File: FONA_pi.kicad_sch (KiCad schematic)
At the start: 37 parts, among them J1 Conn_01x20_Socket, J10 Conn_01x04_Pin, J11 Conn_01x20_Socket, J12 Conn_01x20_Socket, J13 Conn_01x06_Socket, J14 Conn_01x06_Socket, J15 Conn_01x06_Socket, J16 Conn_01x06_Socket, J17 Conn_01x06_Socket, J18 Conn_01x04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

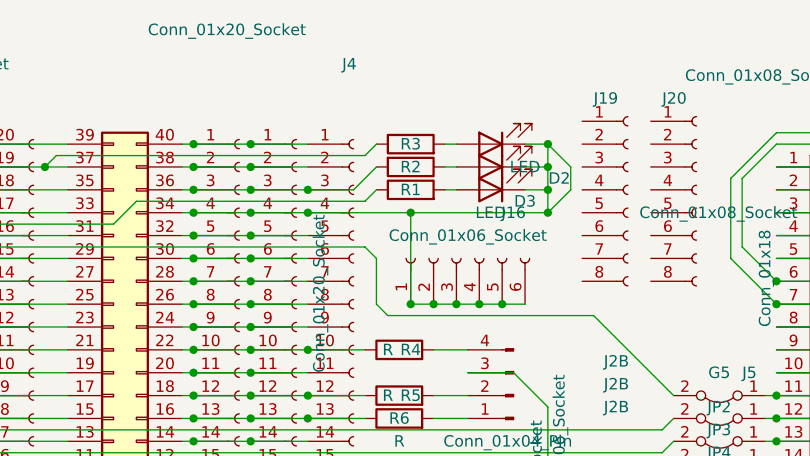
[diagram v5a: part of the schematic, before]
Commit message: Flipped a backwards resistor.  Added labels for LED colors, switch resistors
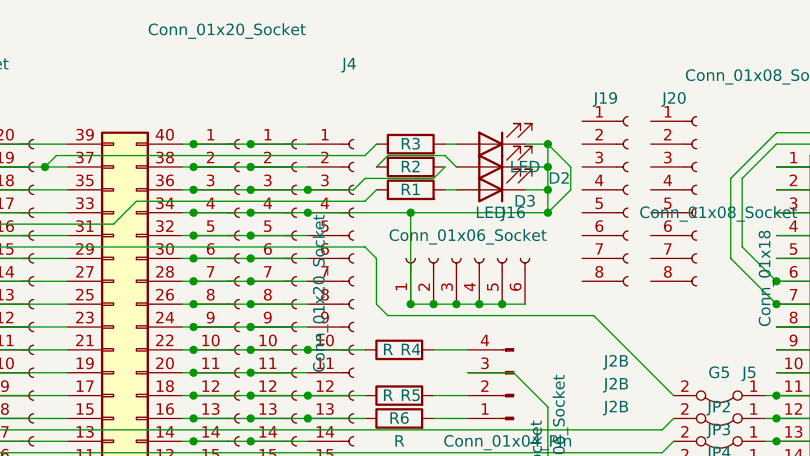
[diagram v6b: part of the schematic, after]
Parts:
- J6: footprint Connector_PinHeader_2.54mm:PinHeader_1x18_P2.54mm_Vertical -> Connector_PinSocket_2.54mm:PinSocket_1x18_P2.54mm_Vertical
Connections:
- net at J2.36 (Pin_36), J3.3 (Pin_3), J4.3 (Pin_3)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: now also R2.1; no longer R2.2
- net at D2.2 (A): now also R2.2; no longer R2.1
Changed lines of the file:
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@@
+    (stroke (width 0) (type default))
+  )
+  (wire (pts (xy 105.41 68.58) (xy 106.68 69.85))
     (stroke (width 0) (type default))
   )
@@
     (stroke (width 0) (type default))
   )
-  (wire (pts (xy 105.41 69.85) (xy 106.68 69.85))
-    (stroke (width 0) (type default))
-  )
   (wire (pts (xy 142.24 87.63) (xy 151.13 87.63))
     (stroke (width 0) (type default))
@@
     (stroke (width 0) (type default))
   )
+  (wire (pts (xy 99.06 68.58) (xy 105.41 68.58))
+    (stroke (width 0) (type default))
+  )
   (wire (pts (xy 97.79 106.68) (xy 102.87 106.68))
     (stroke (width 0) (type default))
@@
     (stroke (width 0) (type default))
   )
+  (wire (pts (xy 96.52 71.12) (xy 95.25 72.39))
+    (stroke (width 0) (type default))
+  )
   (wire (pts (xy 44.45 95.25) (xy 54.61 95.25))
     (stroke (width 0) (type default))
@@
     (stroke (width 0) (type default))
   )
+  (wire (pts (xy 105.41 69.85) (xy 104.14 71.12))
+    (stroke (width 0) (type default))
+  )
   (wire (pts (xy 151.13 77.47) (xy 157.48 77.47))
     (stroke (width 0) (type default))
@@
     (stroke (width 0) (type default))
   )
-  (wire (pts (xy 95.25 72.39) (xy 97.79 69.85))
-    (stroke (width 0) (type default))
-  )
   (wire (pts (xy 46.99 99.06) (xy 45.72 97.79))
     (stroke (width 0) (type default))
@@
     (stroke (width 0) (type default))
   )
+  (wire (pts (xy 104.14 71.12) (xy 96.52 71.12))
+    (stroke (width 0) (type default))
+  )
   (wire (pts (xy 77.47 80.01) (xy 83.82 80.01))
     (stroke (width 0) (type default))
@@
   )
   (wire (pts (xy 76.2 77.47) (xy 77.47 77.47))
+    (stroke (width 0) (type default))
+  )
+  (wire (pts (xy 97.79 69.85) (xy 99.06 68.58))
     (stroke (width 0) (type default))
   )
@@
       (effects (font (size 1.27 1.27)) (justify left))
     )
-    (property "Footprint" "Connector_PinHeader_2.54mm:PinHeader_1x18_P2.54mm_Vertical" (at 156.21 90.17 0)
-      (effects (font (size 1.27 1.27)) hide)
-    )
+    (property "Footprint" "Connector_PinSocket_2.54mm:PinSocket_1x18_P2.54mm_Vertical" (at 156.21 90.17 0)
+      (effects (font (size 1.27 1.27)) hide)
+    )

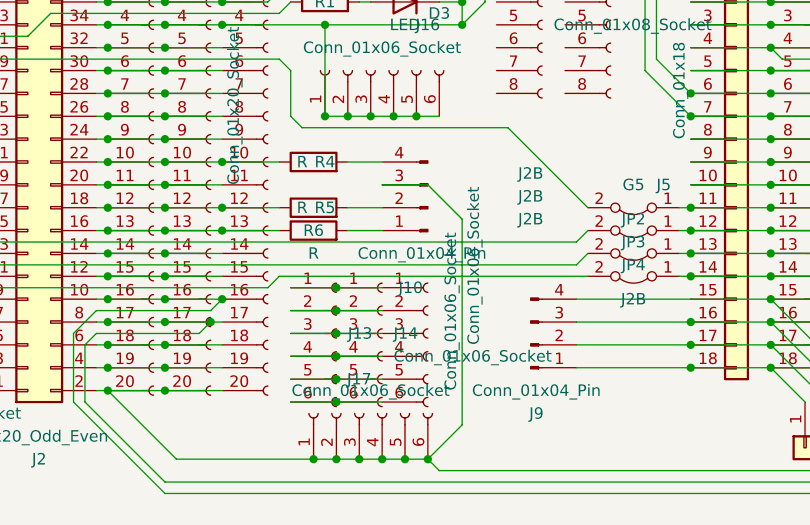
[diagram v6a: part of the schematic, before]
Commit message: Changed which wire of wire harness is used for power.  Now using the first wire from the top, which is a red wire on the harness, so that 5v power will be on the red wire
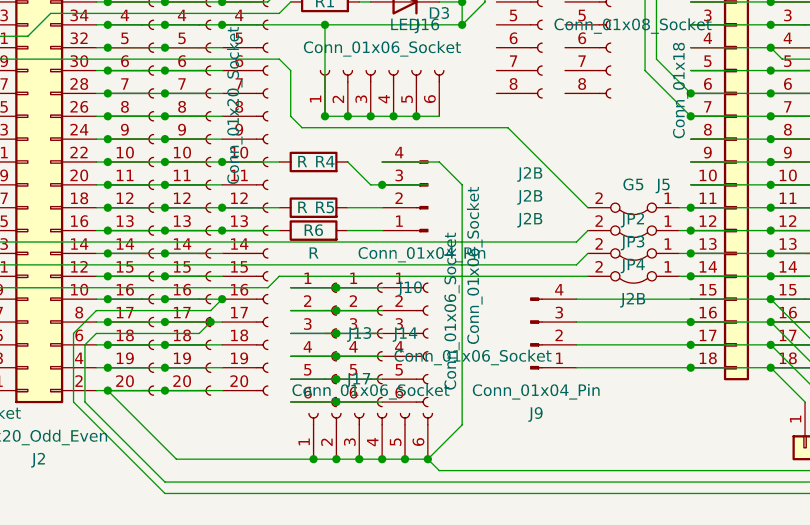
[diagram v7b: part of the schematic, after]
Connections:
- net at J17.1 (Pin_1), J17.2 (Pin_2), J17.3 (Pin_3)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: now also J10.4 (Pin_4); no longer J10.3 (Pin_3)
- net at R4.2: now also J10.3 (Pin_3); no longer J10.4 (Pin_4)
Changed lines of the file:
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@@
   (junction (at 151.13 85.09) (diameter 0) (color 0 0 0 0)
   )
+  (junction (at 107.95 92.71) (diameter 0) (color 0 0 0 0)
+  )
   (junction (at 54.61 105.41) (diameter 0) (color 0 0 0 0)
   )
@@
   (junction (at 83.82 72.39) (diameter 0) (color 0 0 0 0)
   )
-  (wire (pts (xy 104.14 90.17) (xy 107.95 90.17))
-    (stroke (width 0) (type default))
-  )
   (wire (pts (xy 45.72 97.79) (xy 54.61 97.79))
     (stroke (width 0) (type default))
@@
     (stroke (width 0) (type default))
   )
+  (wire (pts (xy 107.95 90.17) (xy 114.3 90.17))
+    (stroke (width 0) (type default))
+  )
   (wire (pts (xy 162.56 127) (xy 83.82 127))
     (stroke (width 0) (type default))
@@
     (stroke (width 0) (type default))
   )
-  (wire (pts (xy 116.84 96.52) (xy 116.84 119.38))
+  (wire (pts (xy 116.84 92.71) (xy 116.84 119.38))
     (stroke (width 0) (type default))
   )
@@
     (stroke (width 0) (type default))
   )
+  (wire (pts (xy 106.68 92.71) (xy 104.14 90.17))
+    (stroke (width 0) (type default))
+  )
   (wire (pts (xy 104.14 95.25) (xy 107.95 95.25))
     (stroke (width 0) (type default))
@@
     (stroke (width 0) (type default))
   )
-  (wire (pts (xy 113.03 92.71) (xy 116.84 96.52))
-    (stroke (width 0) (type default))
-  )
   (wire (pts (xy 137.16 71.12) (xy 142.24 66.04))
     (stroke (width 0) (type default))
@@
     (stroke (width 0) (type default))
   )
+  (wire (pts (xy 114.3 90.17) (xy 116.84 92.71))
+    (stroke (width 0) (type default))
+  )
   (wire (pts (xy 151.13 80.01) (xy 157.48 80.01))
     (stroke (width 0) (type default))
@@
     (stroke (width 0) (type default))
   )
+  (wire (pts (xy 107.95 92.71) (xy 106.68 92.71))
+    (stroke (width 0) (type default))
+  )

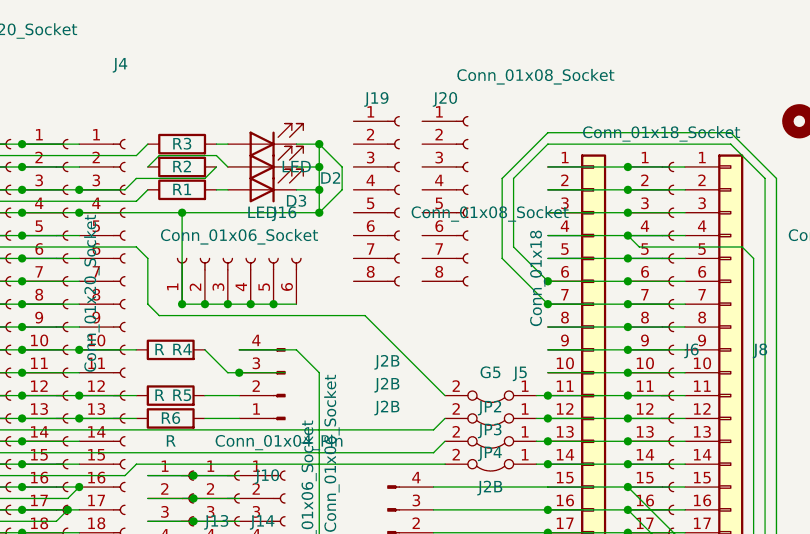
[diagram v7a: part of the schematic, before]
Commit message: Grounded FONA to Pi
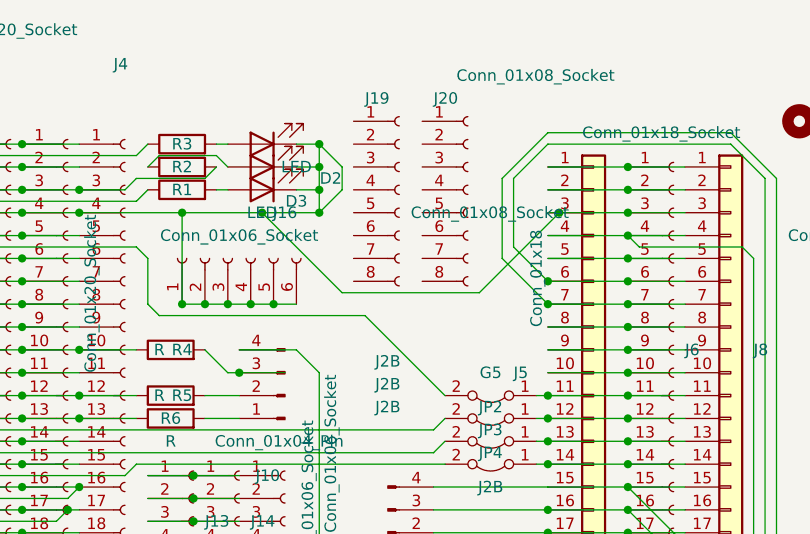
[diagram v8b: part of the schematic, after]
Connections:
- net at D1.1 (K), D2.1 (K), D3.1 (K)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: now also J5.3 (Pin_3), J6.3 (Pin_3), J8.3 (Pin_3)
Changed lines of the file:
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@@
   (junction (at 142.24 100.33) (diameter 0) (color 0 0 0 0)
   )
+  (junction (at 143.51 74.93) (diameter 0) (color 0 0 0 0)
+  )
   (junction (at 44.45 80.01) (diameter 0) (color 0 0 0 0)
   )
@@
   (junction (at 113.03 123.19) (diameter 0) (color 0 0 0 0)
   )
+  (junction (at 110.49 74.93) (diameter 0) (color 0 0 0 0)
+  )
   (junction (at 151.13 110.49) (diameter 0) (color 0 0 0 0)
   )
@@
     (stroke (width 0) (type default))
   )
-  (wire (pts (xy 142.24 74.93) (xy 151.13 74.93))
+  (wire (pts (xy 142.24 74.93) (xy 143.51 74.93))
     (stroke (width 0) (type default))
   )
@@
     (stroke (width 0) (type default))
   )
-  (wire (pts (xy 101.6 74.93) (xy 116.84 74.93))
+  (wire (pts (xy 101.6 74.93) (xy 110.49 74.93))
+    (stroke (width 0) (type default))
+  )
+  (wire (pts (xy 110.49 74.93) (xy 116.84 74.93))
     (stroke (width 0) (type default))
   )
@@
     (stroke (width 0) (type default))
   )
+  (wire (pts (xy 119.38 83.82) (xy 110.49 74.93))
+    (stroke (width 0) (type default))
+  )
   (wire (pts (xy 44.45 69.85) (xy 54.61 69.85))
     (stroke (width 0) (type default))
@@
     (stroke (width 0) (type default))
   )
+  (wire (pts (xy 143.51 74.93) (xy 134.62 83.82))
+    (stroke (width 0) (type default))
+  )
   (wire (pts (xy 54.61 85.09) (xy 63.5 85.09))
     (stroke (width 0) (type default))
@@
     (stroke (width 0) (type default))
   )
+  (wire (pts (xy 119.38 83.82) (xy 134.62 83.82))
+    (stroke (width 0) (type default))
+  )
   (wire (pts (xy 54.61 105.41) (xy 63.5 105.41))
     (stroke (width 0) (type default))
@@
     (stroke (width 0) (type default))
   )
+  (wire (pts (xy 143.51 74.93) (xy 151.13 74.93))
+    (stroke (width 0) (type default))
+  )
